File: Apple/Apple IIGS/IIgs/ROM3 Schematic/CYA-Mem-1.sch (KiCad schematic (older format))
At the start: 28 parts, among them J20 IIgs_Memory_Connector, U6 65SC816

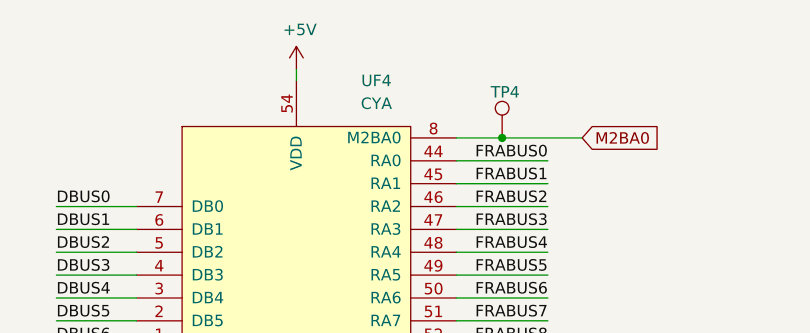
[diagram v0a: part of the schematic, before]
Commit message: Clean-up after detailed circuit analysis - Fixed Reference to library in project file - Fixed BABUS tags on HCT245 (had wrong nets) - Flipped HCT245 circuits on MEGAII page to better match In/Out flow - Changed HCT245 symbol to move enable and DIR to better match In/Out Flow - Changed HCT245 into multi-unit symbol to put VCC/GND pins on Unit B - Fixed MEGAII designator - Fixed ADBUS nets on HCT245 (should be ABUS!) - Added notes with lessons learned from circuit deep-dive
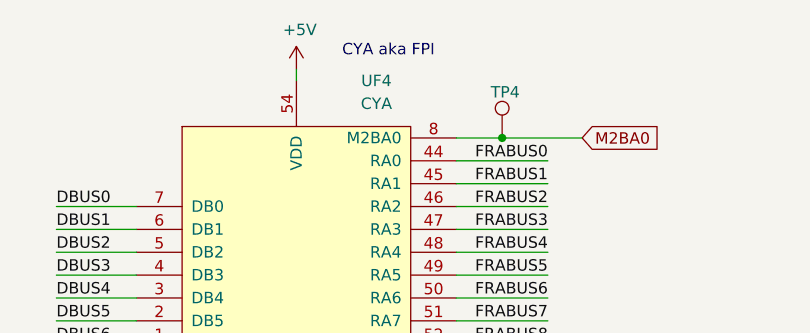
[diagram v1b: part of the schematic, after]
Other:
- note added: "CYA aka FPI"
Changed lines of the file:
@@
 Wire Wire Line
 	5450 900  5450 950
+Text Notes 5650 850  0    50   ~ 0
+CYA aka FPI
 $EndSCHEMATC
